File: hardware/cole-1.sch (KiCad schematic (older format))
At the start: 0 parts

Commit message: Final schematic and PCB layout.
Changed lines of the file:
@@
 F6 "D[0..7]" B R 3950 2250 60
 F7 "RESET" O R 3950 2750 60
-F8 "WATCHDOG" I R 3950 2550 60
-F9 "PHI2" O R 3950 1700 60
-F10 "IRQ" I R 3950 2650 60
-F11 "RWB" O R 3950 1400 60
+F8 "PHI2" O R 3950 1700 60
+F9 "IRQ" I R 3950 2650 60
+F10 "RWB" O R 3950 1400 60
 $EndSheet
 $Sheet
@@
 F6 "IRQ" O R 3950 4100 60
 F7 "RESET" I R 3950 4200 60
-F8 "WATCHDOG" O R 3950 4500 60
-F9 "IOSEL[0..1]" I R 3950 3750 60
+F8 "IOSEL[0..1]" I R 3950 3750 60
 $EndSheet
 Wire Wire Line
@@
 	5050 3550 3950 3550
 Wire Wire Line
-	3950 2550 4850 2550
-Wire Wire Line
-	4850 2550 4850 4500
-Wire Wire Line
-	4850 4500 3950 4500
-Wire Wire Line
 	3950 4100 4700 4100

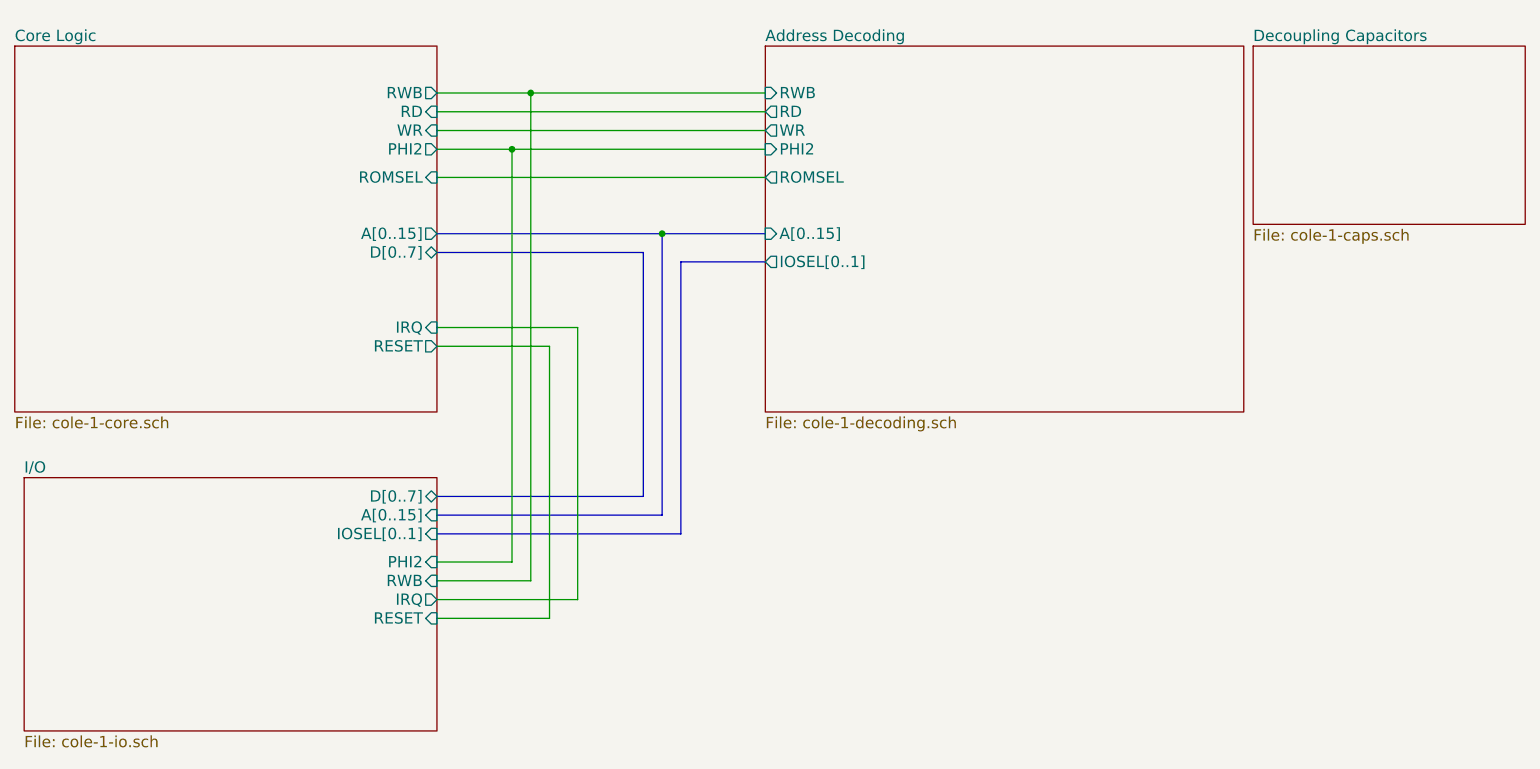
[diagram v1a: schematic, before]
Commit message: Updated schematics, board layout, and GAL code for COLE-1+
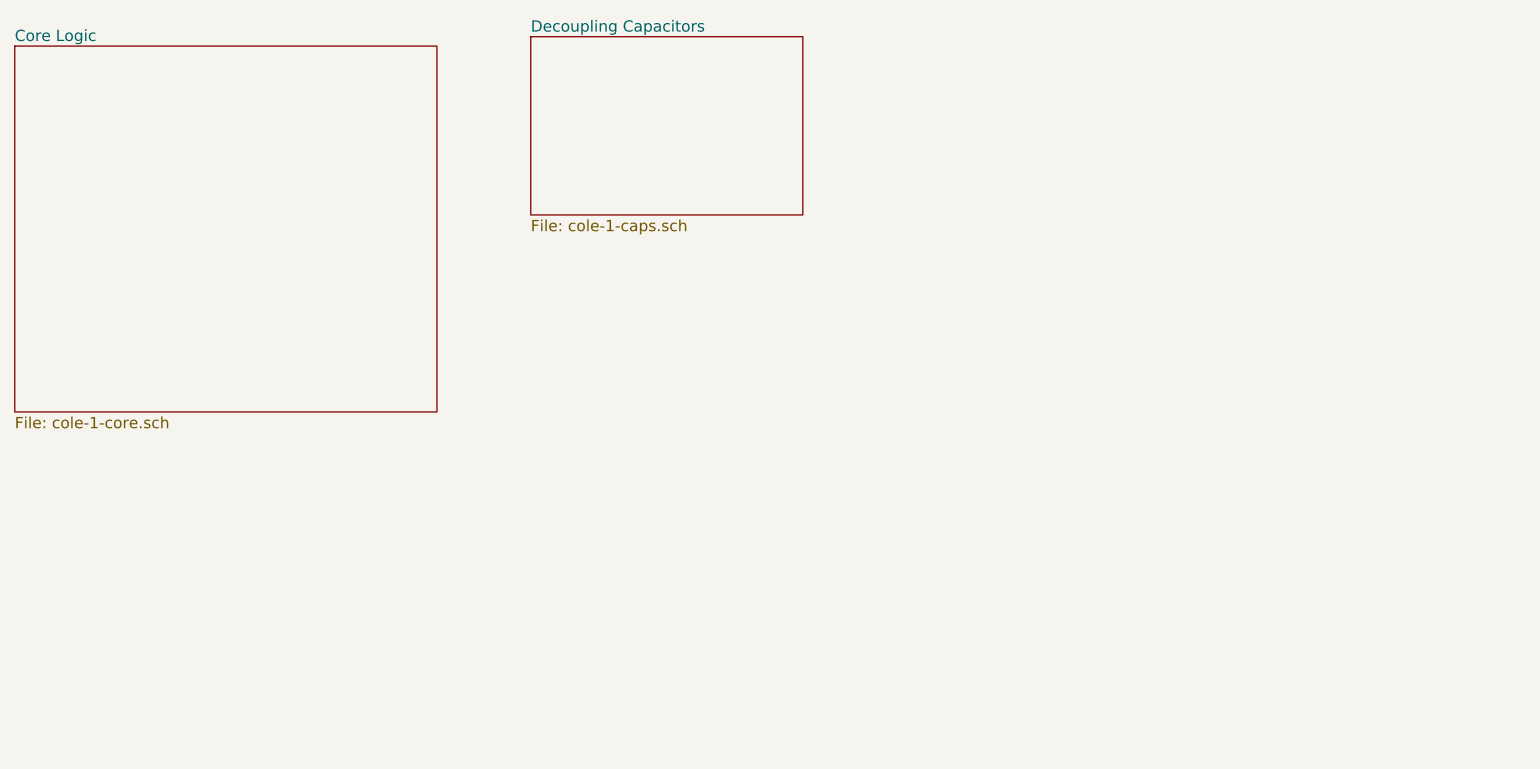
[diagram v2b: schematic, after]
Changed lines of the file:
@@
-EESchema Schematic File Version 2
-LIBS:power
-LIBS:device
-LIBS:switches
-LIBS:relays
-LIBS:motors
-LIBS:transistors
-LIBS:conn
-LIBS:linear
-LIBS:regul
-LIBS:74xx
-LIBS:cmos4000
-LIBS:adc-dac
-LIBS:memory
-LIBS:xilinx
-LIBS:microcontrollers
-LIBS:dsp
-LIBS:microchip
-LIBS:analog_switches
-LIBS:motorola
-LIBS:texas
-LIBS:intel
-LIBS:audio
-LIBS:interface
-LIBS:digital-audio
-LIBS:philips
-LIBS:display
-LIBS:cypress
-LIBS:siliconi
-LIBS:opto
-LIBS:atmel
-LIBS:contrib
-LIBS:valves
-LIBS:65xx
-LIBS:MAX1232
-LIBS:osc
-LIBS:cole-1-cache
-EELAYER 25 0
+EESchema Schematic File Version 4
+EELAYER 30 0
 EELAYER END
 $Descr A4 11693 8268
 encoding utf-8
-Sheet 1 5
+Sheet 1 3
 Title ""
 Date ""
@@
 $EndDescr
 $Sheet
+S 4450 1100 1450 950
+U 5A482044
+F0 "Decoupling Capacitors" 60
+F1 "cole-1-caps.sch" 60
+$EndSheet
+$Sheet
 S 1700 1150 2250 1950
 U 5A457B7F
 F0 "Core Logic" 60
 F1 "cole-1-core.sch" 60
-F2 "ROMSEL" I R 3950 1850 60
-F3 "RD" I R 3950 1500 60
-F4 "WR" I R 3950 1600 60
-F5 "A[0..15]" O R 3950 2150 60
-F6 "D[0..7]" B R 3950 2250 60
-F7 "RESET" O R 3950 2750 60
-F8 "PHI2" O R 3950 1700 60
-F9 "IRQ" I R 3950 2650 60
-F10 "RWB" O R 3950 1400 60
 $EndSheet
-$Sheet
-S 5700 1150 2550 1950
-U 5A459B30
-F0 "Address Decoding" 60
-F1 "cole-1-decoding.sch" 60
-F2 "RWB" I L 5700 1400 60
-F3 "PHI2" I L 5700 1700 60
-F4 "A[0..15]" I L 5700 2150 60
-F5 "RD" O L 5700 1500 60
-F6 "WR" O L 5700 1600 60
-F7 "ROMSEL" O L 5700 1850 60
-F8 "IOSEL[0..1]" O L 5700 2300 60
-$EndSheet
-$Sheet
-S 1750 3450 2200 1350
-U 5A46207D
-F0 "I/O" 60
-F1 "cole-1-io.sch" 60
-F2 "A[0..15]" I R 3950 3650 60
-F3 "D[0..7]" B R 3950 3550 60
-F4 "PHI2" I R 3950 3900 60
-F5 "RWB" I R 3950 4000 60
-F6 "IRQ" O R 3950 4100 60
-F7 "RESET" I R 3950 4200 60
-F8 "IOSEL[0..1]" I R 3950 3750 60
-$EndSheet
-Wire Wire Line
-	3950 1850 5700 1850
-Wire Wire Line
-	3950 1400 5700 1400
-Wire Wire Line
-	5700 1500 3950 1500
-Wire Wire Line
-	5700 1600 3950 1600
-Wire Wire Line
-	3950 1700 5700 1700
-Wire Bus Line
-	3950 2150 5700 2150
-Wire Bus Line
-	3950 2250 5050 2250
-Wire Bus Line
-	5050 2250 5050 3550
-Wire Bus Line
-	5050 3550 3950 3550
-Wire Wire Line
-	3950 4100 4700 4100
-Wire Wire Line
-	4700 4100 4700 2650
-Wire Wire Line
-	4700 2650 3950 2650
-Wire Wire Line
-	3950 2750 4550 2750
-Wire Wire Line
-	4550 2750 4550 4200
-Wire Wire Line
-	4550 4200 3950 4200
-Wire Wire Line
-	3950 4000 4450 4000
-Wire Wire Line
-	4450 4000 4450 1400
-Connection ~ 4450 1400
-Wire Wire Line
-	3950 3900 4350 3900
-Wire Wire Line
-	4350 3900 4350 1700
-Connection ~ 4350 1700
-Wire Bus Line
-	3950 3650 5150 3650
-Wire Bus Line
-	5150 3650 5150 2150
-Connection ~ 5150 2150
-$Sheet
-S 8300 1150 1450 950
-U 5A482044
-F0 "Decoupling Capacitors" 60
-F1 "cole-1-caps.sch" 60
-$EndSheet
-Wire Bus Line
-	5700 2300 5250 2300
-Wire Bus Line
-	5250 2300 5250 3750
-Wire Bus Line
-	5250 3750 3950 3750
 $EndSCHEMATC
